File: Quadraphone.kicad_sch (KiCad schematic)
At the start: 29 parts, among them J1 Conn_01x10_Male, J2 Conn_01x10_Male, J3 Conn_01x10_Male, J4 Conn_01x10_Male, J5 Eurorack_10_pin_power, U1 AMS1117-5.0, U14 LM4040DBZ-2.5, U3 MCP6002, U4 LM4040DBZ-5, U5 MCP6004, U8 4066

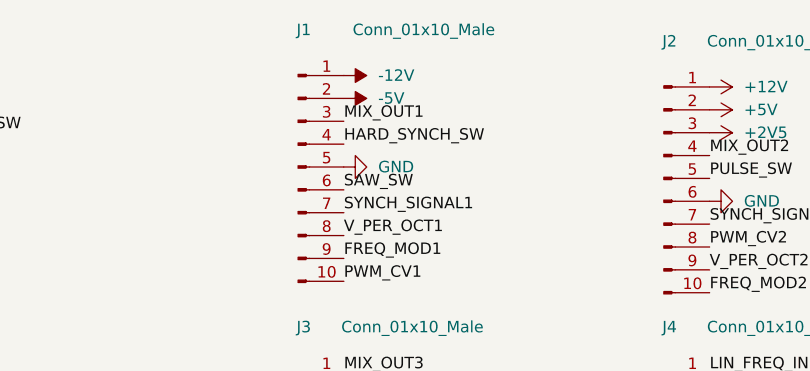
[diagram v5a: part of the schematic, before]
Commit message: Routing power rails
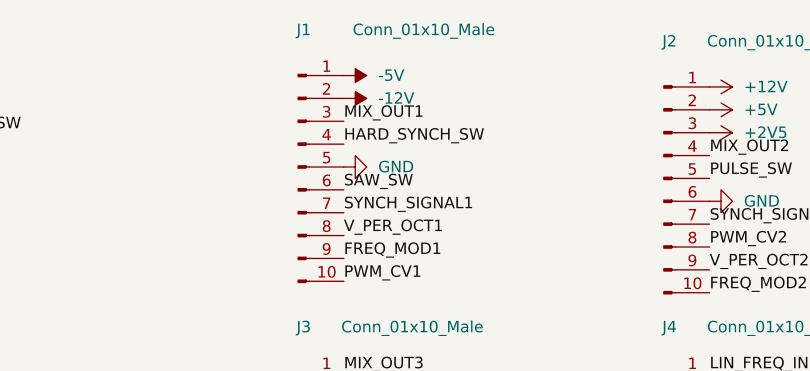
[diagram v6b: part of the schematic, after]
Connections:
- net -12V: now also J1.2 (Pin_2); no longer J1.1 (Pin_1)
- net -5V: now also J1.1 (Pin_1); no longer J1.2 (Pin_2)
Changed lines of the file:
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@@
     (pin "1")
   )
-  (symbol (lib_id "power:-5V") (at 212.09 27.94 270) (unit 1)
-    (in_bom yes) (on_board yes) (fields_autoplaced)
-    (property "Reference" "#PWR0104" (id 0) (at 214.63 27.94 0)
-      (effects (font (size 1.27 1.27)) hide)
-    )
-    (property "Value" "-5V" (id 1) (at 215.9 27.9399 90)
-      (effects (font (size 1.27 1.27)) (justify left))
-    )
-    (property "Footprint" "" (id 2) (at 212.09 27.94 0)
-      (effects (font (size 1.27 1.27)) hide)
-    )
-    (property "Datasheet" "" (id 3) (at 212.09 27.94 0)
+  (symbol (lib_id "power:-5V") (at 212.09 25.4 270) (unit 1)
+    (in_bom yes) (on_board yes) (fields_autoplaced)
+    (property "Reference" "#PWR0104" (id 0) (at 214.63 25.4 0)
+      (effects (font (size 1.27 1.27)) hide)
+    )
+    (property "Value" "-5V" (id 1) (at 215.9 25.3999 90)
+      (effects (font (size 1.27 1.27)) (justify left))
+    )
+    (property "Footprint" "" (id 2) (at 212.09 25.4 0)
+      (effects (font (size 1.27 1.27)) hide)
+    )
+    (property "Datasheet" "" (id 3) (at 212.09 25.4 0)
       (effects (font (size 1.27 1.27)) hide)
     )
@@
     (pin "2")
   )
-  (symbol (lib_id "power:-12V") (at 212.09 25.4 270) (unit 1)
-    (in_bom yes) (on_board yes) (fields_autoplaced)
-    (property "Reference" "#PWR041" (id 0) (at 214.63 25.4 0)
-      (effects (font (size 1.27 1.27)) hide)
-    )
-    (property "Value" "-12V" (id 1) (at 215.9 25.3999 90)
-      (effects (font (size 1.27 1.27)) (justify left))
-    )
-    (property "Footprint" "" (id 2) (at 212.09 25.4 0)
-      (effects (font (size 1.27 1.27)) hide)
-    )
-    (property "Datasheet" "" (id 3) (at 212.09 25.4 0)
-      (effects (font (size 1.27 1.27)) hide)
-    )
+  (symbol (lib_id "power:-12V") (at 212.09 27.94 270) (unit 1)
+    (in_bom yes) (on_board yes) (fields_autoplaced)
+    (property "Reference" "#PWR041" (id 0) (at 214.63 27.94 0)
+      (effects (font (size 1.27 1.27)) hide)
+    )
+    (property "Value" "-12V" (id 1) (at 215.9 27.9399 90)
+      (effects (font (size 1.27 1.27)) (justify left))
+    )
+    (property "Footprint" "" (id 2) (at 212.09 27.94 0)
+      (effects (font (size 1.27 1.27)) hide)
+    )
+    (property "Datasheet" "" (id 3) (at 212.09 27.94 0)
+      (effects (font (size 1.27 1.27)) hide)
+    )
